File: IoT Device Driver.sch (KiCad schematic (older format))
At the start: 10 parts

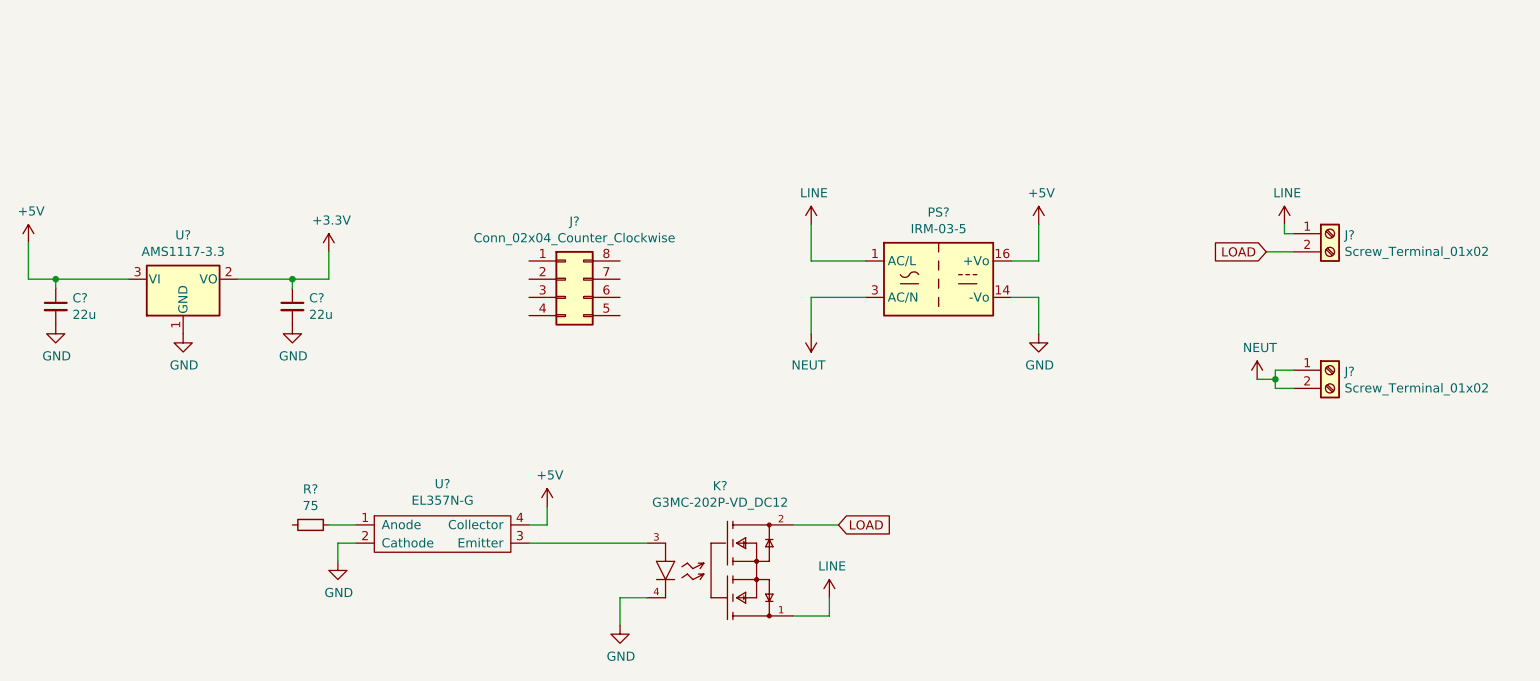
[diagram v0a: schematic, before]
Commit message: assignment of footprint over except optocoupler
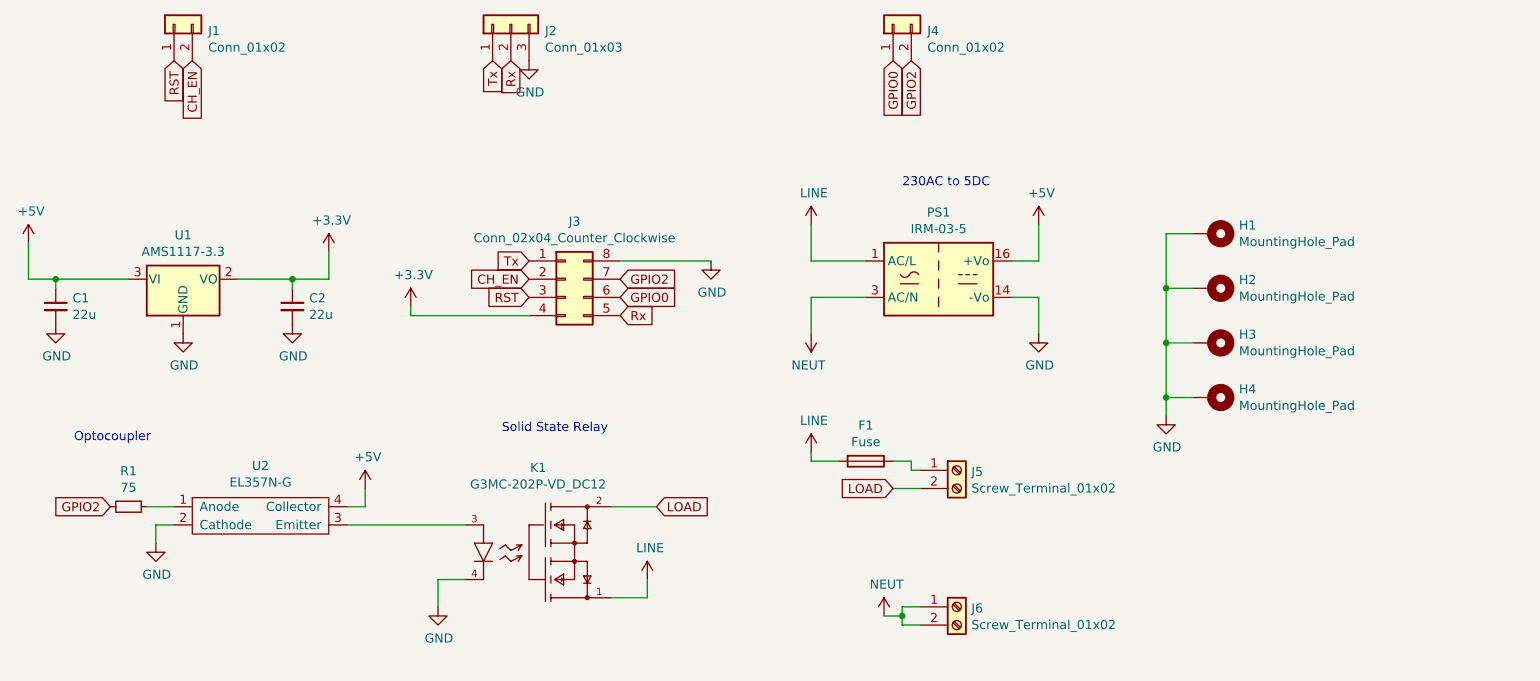
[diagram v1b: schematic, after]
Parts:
- added F1: Fuse, Fuse:Fuseholder_Cylinder-5x20mm_EATON_H15-V-1_Vertical_Closed, symbol Device:Fuse
- added H1, H2, H3, H4: MountingHole_Pad, MountingHole:MountingHole_4.3mm_M4_Pad_Via, symbol Mechanical:MountingHole_Pad
- added J1, J4: Conn_01x02, Connector_PinHeader_2.54mm:PinHeader_1x02_P2.54mm_Vertical, symbol Connector_Generic:Conn_01x02
- added J2: Conn_01x03, Connector_PinHeader_2.54mm:PinHeader_1x03_P2.54mm_Vertical, symbol Connector_Generic:Conn_01x03
- C1, C2: renamed from C?; footprint (none) -> Capacitor_SMD:C_0603_1608Metric
- J3: renamed from J?; footprint (none) -> Connector_PinHeader_2.54mm:PinHeader_2x04_P2.54mm_Vertical
- J5, J6: renamed from J?; footprint (none) -> TerminalBlock_Phoenix:TerminalBlock_Phoenix_PT-1,5-2-5.0-H_1x02_P5.00mm_Horizontal
- R1: renamed from R?; footprint (none) -> Resistor_SMD:R_1206_3216Metric
- gave numbers to parts that had none: 4
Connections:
- net +3V3: now also J3.4 (Pin_4)
- net GND: now also J3.8 (Pin_8), H1.1, H2.1, H3.1, H4.1, J2.3 (Pin_3)
- net LINE: now also F1.2; no longer J5.1 (Pin_1)
- net Tx: now reaches J3.1 (Pin_1)
- net Tx: now also J2.1 (Pin_1)
- net CH_EN: now reaches J3.2 (Pin_2)
- net CH_EN: now also J1.2 (Pin_2)
- net RST: now reaches J3.3 (Pin_3)
- net RST: now also J1.1 (Pin_1)
- net Rx: now reaches J3.5 (Pin_5)
- net Rx: now also J2.2 (Pin_2)
- net GPIO0: now reaches J3.6 (Pin_6)
- net GPIO0: now also J4.1 (Pin_1)
- net GPIO2: now reaches J3.7 (Pin_7)
- net GPIO2: now also R1.2, J4.2 (Pin_2)
- new net: F1.1, J5.1 (Pin_1)
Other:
- note added: "230AC to 5DC"
- note added: "Optocoupler"
- note added: "Solid State Relay"
- moved on the sheet: J5, J6, K1, R1, U2

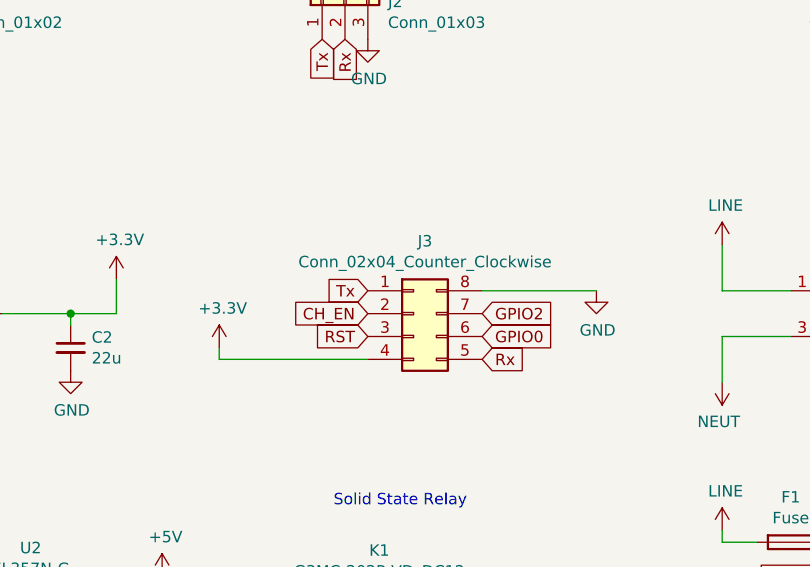
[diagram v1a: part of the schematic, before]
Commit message: Components alignment in PCB
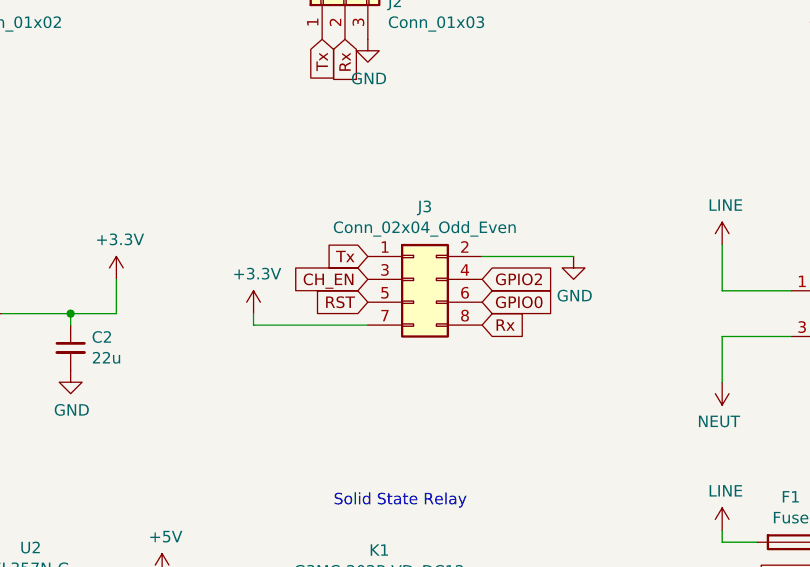
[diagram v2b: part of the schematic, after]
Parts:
- removed J3: Conn_02x04_Counter_Clockwise, Connector_PinHeader_2.54mm:PinHeader_2x04_P2.54mm_Vertical, symbol Connector_Generic:Conn_02x04_Counter_Clockwise
- added J3: Conn_02x04_Odd_Even, Connector_PinHeader_2.54mm:PinHeader_2x04_P2.54mm_Vertical, symbol Connector_Generic:Conn_02x04_Odd_Even
- F1: footprint Fuse:Fuseholder_Cylinder-5x20mm_EATON_H15-V-1_Vertical_Closed -> Fuse:Fuseholder_Cylinder-5x20mm_Schurter_0031_8201_Horizontal_Open
- K1: footprint Omron-G3MC-202P-VD_DC12-* -> eec:Omron-G3MC-202P-VD_DC12-MFG
- U2: footprint (none) -> saranyan:EL357N_G-2.54SOP4P
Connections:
- net +3V3: now also J3.7 (Pin_7)
- net CH_EN: now also J3.3 (Pin_3)
- net GND: now also J3.2 (Pin_2)
- net GPIO0: now also J3.6 (Pin_6)
- net GPIO2: now also J3.4 (Pin_4)
- net RST: now also J3.5 (Pin_5)
- net Rx: now also J3.8 (Pin_8)
- net Tx: now also J3.1 (Pin_1)
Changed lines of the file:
@@
 $EndDescr
-$Comp
-L Connector_Generic:Conn_02x04_Counter_Clockwise J3
-U 1 1 6144891D
-P 5100 3200
-F 0 "J3" H 5150 3517 50  0000 C CNN
-F 1 "Conn_02x04_Counter_Clockwise" H 5150 3426 50  0000 C CNN
-F 2 "Connector_PinHeader_2.54mm:PinHeader_2x04_P2.54mm_Vertical" H 5100 3200 50  0001 C CNN
-F 3 "~" H 5100 3200 50  0001 C CNN
-	1    5100 3200
-	1    0    0    -1
-$EndComp
 $Comp
 L Regulator_Linear:AMS1117-3.3 U1
@@
 F 0 "K1" H 4950 4864 50  0000 C CNN
 F 1 "G3MC-202P-VD_DC12" H 4950 4773 50  0000 C CNN
-F 2 "Omron-G3MC-202P-VD_DC12-*" H 4450 5050 50  0001 L CNN
+F 2 "eec:Omron-G3MC-202P-VD_DC12-MFG" H 4450 5050 50  0001 L CNN
 F 3 "https://omronfs.omron.com/en_US/ecb/products/pdf/en-g3mc.pdf" H 4450 5150 50  0001 L CNN
 F 4 "+80°C" H 4450 5250 50  0001 L CNN "ambient temperature range high"
@@
 F 0 "U2" H 3425 4775 50  0000 C CNN
 F 1 "EL357N-G" H 3425 4684 50  0000 C CNN
-F 2 "" H 3400 4500 50  0001 C CNN
+F 2 "saranyan:EL357N_G-2.54SOP4P" H 3400 4500 50  0001 C CNN
 F 3 "" H 3400 4500 50  0001 C CNN
 	1    3400 4500
@@
 Wire Wire Line
 	6900 4350 7050 4350
-$Comp
-L power:+3.3V #PWR08
-U 1 1 6148FED5
-P 4250 3350
-F 0 "#PWR08" H 4250 3200 50  0001 C CNN
-F 1 "+3.3V" H 4265 3523 50  0000 C CNN
-F 2 "" H 4250 3350 50  0001 C CNN
-F 3 "" H 4250 3350 50  0001 C CNN
-	1    4250 3350
-	1    0    0    -1
-$EndComp
-Wire Wire Line
-	4250 3350 4250 3400
-Wire Wire Line
-	4250 3400 4900 3400
 Text GLabel 4700 2000 3    50   Input ~ 0
-Tx
-Text GLabel 4900 3100 0    50   Input ~ 0
 Tx
 Text GLabel 4800 2000 3    50   Input ~ 0
 Rx
-Text GLabel 5400 3400 2    50   Input ~ 0
-Rx
 Text GLabel 6900 2000 3    50   Input ~ 0
-GPIO0
-Text GLabel 5400 3300 2    50   Input ~ 0
 GPIO0
 Text GLabel 7000 2000 3    50   Input ~ 0
 GPIO2
-Text GLabel 5400 3200 2    50   Input ~ 0
-GPIO2
 Text GLabel 2600 4450 0    50   Input ~ 0
 GPIO2
-Text GLabel 4900 3300 0    50   Input ~ 0
-RST
-$Comp
-L power:GND #PWR012
-U 1 1 61495F70
-P 5900 3100
-F 0 "#PWR012" H 5900 2850 50  0001 C CNN
-F 1 "GND" H 5905 2927 50  0000 C CNN
-F 2 "" H 5900 3100 50  0001 C CNN
-F 3 "" H 5900 3100 50  0001 C CNN
-	1    5900 3100
-	1    0    0    -1
-$EndComp
-Wire Wire Line
-	5400 3100 5900 3100
-Text GLabel 4900 3200 0    50   Input ~ 0
-CH_EN
 Text GLabel 2950 2000 3    50   Input ~ 0
 RST
@@
 F 0 "F1" V 6553 4200 50  0000 C CNN
 F 1 "Fuse" V 6644 4200 50  0000 C CNN
-F 2 "Fuse:Fuseholder_Cylinder-5x20mm_EATON_H15-V-1_Vertical_Closed" V 6680 4200 50  0001 C CNN
+F 2 "Fuse:Fuseholder_Cylinder-5x20mm_Schurter_0031_8201_Horizontal_Open" V 6680 4200 50  0001 C CNN
 F 3 "~" H 6750 4200 50  0001 C CNN
 	1    6750 4200
@@
 Wire Wire Line
 	6900 4200 7000 4200
+Text GLabel 4900 3150 0    50   Input ~ 0
+RST
+$Comp
+L Connector_Generic:Conn_02x04_Odd_Even J3
+U 1 1 614E39E6
+P 5100 3050
+F 0 "J3" H 5150 3367 50  0000 C CNN
+F 1 "Conn_02x04_Odd_Even" H 5150 3276 50  0000 C CNN
+F 2 "Connector_PinHeader_2.54mm:PinHeader_2x04_P2.54mm_Vertical" H 5100 3050 50  0001 C CNN
+F 3 "~" H 5100 3050 50  0001 C CNN
+	1    5100 3050
+	1    0    0    -1
+$EndComp
+Text GLabel 4900 2950 0    50   Input ~ 0
+Tx
+Text GLabel 4900 3050 0    50   Input ~ 0
+CH_EN
+$Comp
+L power:+3.3V #PWR08
+U 1 1 614E4A4D
+P 4400 3200
+F 0 "#PWR08" H 4400 3050 50  0001 C CNN
+F 1 "+3.3V" H 4415 3373 50  0000 C CNN
+F 2 "" H 4400 3200 50  0001 C CNN
+F 3 "" H 4400 3200 50  0001 C CNN
+	1    4400 3200
+	1    0    0    -1
+$EndComp
+Text GLabel 5400 3050 2    50   Input ~ 0
+GPIO2
+Text GLabel 5400 3150 2    50   Input ~ 0
+GPIO0
+Text GLabel 5400 3250 2    50   Input ~ 0
+Rx
+$Comp
+L power:GND #PWR012
+U 1 1 614E6EBE
+P 5800 2950
+F 0 "#PWR012" H 5800 2700 50  0001 C CNN
+F 1 "GND" H 5805 2777 50  0000 C CNN
+F 2 "" H 5800 2950 50  0001 C CNN
+F 3 "" H 5800 2950 50  0001 C CNN
+	1    5800 2950
+	1    0    0    -1
+$EndComp
+Wire Wire Line
+	5400 2950 5800 2950
+Wire Wire Line
+	4400 3200 4400 3250
+Wire Wire Line
+	4400 3250 4900 3250
 $EndSCHEMATC

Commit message: Routing
Routing for low power components over. Things to do: 1)Edit copper fill area, 2(Calculate track width for 3A, 3)Lay track for high power components on bottom layer only
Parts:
- PS1: footprint Converter_ACDC:Converter_ACDC_MeanWell_IRM-03-xx_THT -> Converter_ACDC:Converter_ACDC_MeanWell_IRM-03-xx_SMD
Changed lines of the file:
@@
 F 0 "PS1" H 7150 3567 50  0000 C CNN
 F 1 "IRM-03-5" H 7150 3476 50  0000 C CNN
-F 2 "Converter_ACDC:Converter_ACDC_MeanWell_IRM-03-xx_THT" H 7150 2850 50  0001 C CNN
+F 2 "Converter_ACDC:Converter_ACDC_MeanWell_IRM-03-xx_SMD" H 7150 2850 50  0001 C CNN
 F 3 "https://www.meanwell.com/Upload/PDF/IRM-03/IRM-03-SPEC.PDF" H 7150 2800 50  0001 C CNN
 	1    7150 3200

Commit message: PCB Version 1.0 over
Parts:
- added J7: Conn_01x06, Connector_PinSocket_2.54mm:PinSocket_1x06_P2.54mm_Vertical, symbol Connector_Generic:Conn_01x06
- J1, J4: footprint Connector_PinHeader_2.54mm:PinHeader_1x02_P2.54mm_Vertical -> Connector_PinSocket_2.54mm:PinSocket_1x02_P2.54mm_Vertical
- J2: footprint Connector_PinHeader_2.54mm:PinHeader_1x03_P2.54mm_Vertical -> Connector_PinSocket_2.54mm:PinSocket_1x03_P2.54mm_Vertical
- K1: value G3MC-202P-VD_DC12 -> G3MC-202P-VD_DC5
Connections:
- net +3V3: now also J7.3 (Pin_3), J7.4 (Pin_4)
- net +5V: now also J7.1 (Pin_1), J7.2 (Pin_2)
- net GND: now also J7.5 (Pin_5), J7.6 (Pin_6)
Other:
- moved on the sheet: J1, J2, J4
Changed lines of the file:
@@
 P 4450 4550
 F 0 "K1" H 4950 4864 50  0000 C CNN
-F 1 "G3MC-202P-VD_DC12" H 4950 4773 50  0000 C CNN
+F 1 "G3MC-202P-VD_DC5" H 4950 4773 50  0000 C CNN
 F 2 "eec:Omron-G3MC-202P-VD_DC12-MFG" H 4450 5050 50  0001 L CNN
 F 3 "https://omronfs.omron.com/en_US/ecb/products/pdf/en-g3mc.pdf" H 4450 5150 50  0001 L CNN
@@
 Wire Wire Line
 	6900 4350 7050 4350
-Text GLabel 4700 2000 3    50   Input ~ 0
+Text GLabel 3900 2000 3    50   Input ~ 0
 Tx
-Text GLabel 4800 2000 3    50   Input ~ 0
+Text GLabel 4000 2000 3    50   Input ~ 0
 Rx
-Text GLabel 6900 2000 3    50   Input ~ 0
+Text GLabel 5200 2000 3    50   Input ~ 0
 GPIO0
-Text GLabel 7000 2000 3    50   Input ~ 0
+Text GLabel 5300 2000 3    50   Input ~ 0
 GPIO2
 Text GLabel 2600 4450 0    50   Input ~ 0
 GPIO2
-Text GLabel 2950 2000 3    50   Input ~ 0
+Text GLabel 2500 2000 3    50   Input ~ 0
 RST
-Text GLabel 3050 2000 3    50   Input ~ 0
+Text GLabel 2600 2000 3    50   Input ~ 0
 CH_EN
 $Comp
 L power:GND #PWR010
 U 1 1 614974B0
-P 4900 2000
-F 0 "#PWR010" H 4900 1750 50  0001 C CNN
-F 1 "GND" H 4905 1827 50  0000 C CNN
-F 2 "" H 4900 2000 50  0001 C CNN
-F 3 "" H 4900 2000 50  0001 C CNN
-	1    4900 2000
+P 4100 2000
+F 0 "#PWR010" H 4100 1750 50  0001 C CNN
+F 1 "GND" H 4105 1827 50  0000 C CNN
+F 2 "" H 4100 2000 50  0001 C CNN
+F 3 "" H 4100 2000 50  0001 C CNN
+	1    4100 2000
 	1    0    0    -1
 $EndComp
@@
 L Connector_Generic:Conn_01x02 J1
 U 1 1 614A936D
-P 2950 1800
-F 0 "J1" V 2914 1612 50  0000 R CNN
-F 1 "Conn_01x02" V 2823 1612 50  0000 R CNN
-F 2 "Connector_PinHeader_2.54mm:PinHeader_1x02_P2.54mm_Vertical" H 2950 1800 50  0001 C CNN
-F 3 "~" H 2950 1800 50  0001 C CNN
-	1    2950 1800
+P 2500 1800
+F 0 "J1" V 2464 1612 50  0000 R CNN
+F 1 "Conn_01x02" V 2373 1612 50  0000 R CNN
+F 2 "Connector_PinSocket_2.54mm:PinSocket_1x02_P2.54mm_Vertical" H 2500 1800 50  0001 C CNN
+F 3 "~" H 2500 1800 50  0001 C CNN
+	1    2500 1800
 	0    -1   -1   0
 $EndComp
@@
 L Connector_Generic:Conn_01x02 J4
 U 1 1 614A9BB4
-P 6900 1800
-F 0 "J4" V 6864 1612 50  0000 R CNN
-F 1 "Conn_01x02" V 6773 1612 50  0000 R CNN
-F 2 "Connector_PinHeader_2.54mm:PinHeader_1x02_P2.54mm_Vertical" H 6900 1800 50  0001 C CNN
-F 3 "~" H 6900 1800 50  0001 C CNN
-	1    6900 1800
+P 5200 1800
+F 0 "J4" V 5164 1612 50  0000 R CNN
+F 1 "Conn_01x02" V 5073 1612 50  0000 R CNN
+F 2 "Connector_PinSocket_2.54mm:PinSocket_1x02_P2.54mm_Vertical" H 5200 1800 50  0001 C CNN
+F 3 "~" H 5200 1800 50  0001 C CNN
+	1    5200 1800
 	0    -1   -1   0
 $EndComp
@@
 L Connector_Generic:Conn_01x03 J2
 U 1 1 614AA5E9
-P 4800 1800
-F 0 "J2" V 4764 1612 50  0000 R CNN
-F 1 "Conn_01x03" V 4673 1612 50  0000 R CNN
-F 2 "Connector_PinHeader_2.54mm:PinHeader_1x03_P2.54mm_Vertical" H 4800 1800 50  0001 C CNN
-F 3 "~" H 4800 1800 50  0001 C CNN
-	1    4800 1800
+P 4000 1800
+F 0 "J2" V 3964 1612 50  0000 R CNN
+F 1 "Conn_01x03" V 3873 1612 50  0000 R CNN
+F 2 "Connector_PinSocket_2.54mm:PinSocket_1x03_P2.54mm_Vertical" H 4000 1800 50  0001 C CNN
+F 3 "~" H 4000 1800 50  0001 C CNN
+	1    4000 1800
 	0    -1   -1   0
 $EndComp
@@
 Wire Wire Line
 	4400 3250 4900 3250
+$Comp
+L Connector_Generic:Conn_01x06 J7
+U 1 1 6151AA3C
+P 6700 1800
+F 0 "J7" V 6664 1412 50  0000 R CNN
+F 1 "Conn_01x06" V 6573 1412 50  0000 R CNN
+F 2 "Connector_PinSocket_2.54mm:PinSocket_1x06_P2.54mm_Vertical" H 6700 1800 50  0001 C CNN
+F 3 "~" H 6700 1800 50  0001 C CNN
+	1    6700 1800
+	0    -1   -1   0
+$EndComp
+$Comp
+L power:+3.3V #PWR022
+U 1 1 6151C48B
+P 6700 2100
+F 0 "#PWR022" H 6700 1950 50  0001 C CNN
+F 1 "+3.3V" V 6700 2350 50  0000 C CNN
+F 2 "" H 6700 2100 50  0001 C CNN
+F 3 "" H 6700 2100 50  0001 C CNN
+	1    6700 2100
+	-1   0    0    1
+$EndComp
+$Comp
+L power:+3.3V #PWR023
+U 1 1 6151F1E6
+P 6800 2100
+F 0 "#PWR023" H 6800 1950 50  0001 C CNN
+F 1 "+3.3V" V 6800 2350 50  0000 C CNN
+F 2 "" H 6800 2100 50  0001 C CNN
+F 3 "" H 6800 2100 50  0001 C CNN
+	1    6800 2100
+	-1   0    0    1
+$EndComp
+$Comp
+L power:+5V #PWR021
+U 1 1 6151F7D4
+P 6600 2100
+F 0 "#PWR021" H 6600 1950 50  0001 C CNN
+F 1 "+5V" V 6600 2300 50  0000 C CNN
+F 2 "" H 6600 2100 50  0001 C CNN
+F 3 "" H 6600 2100 50  0001 C CNN
+	1    6600 2100
+	-1   0    0    1
+$EndComp
+$Comp
+L power:+5V #PWR020
+U 1 1 61520689
+P 6500 2100
+F 0 "#PWR020" H 6500 1950 50  0001 C CNN
+F 1 "+5V" V 6500 2300 50  0000 C CNN
+F 2 "" H 6500 2100 50  0001 C CNN
+F 3 "" H 6500 2100 50  0001 C CNN
+	1    6500 2100
+	-1   0    0    1
+$EndComp
+$Comp
+L power:GND #PWR024
+U 1 1 6152252F
+P 6900 2100
+F 0 "#PWR024" H 6900 1850 50  0001 C CNN
+F 1 "GND" V 6900 1900 50  0000 C CNN
+F 2 "" H 6900 2100 50  0001 C CNN
+F 3 "" H 6900 2100 50  0001 C CNN
+	1    6900 2100
+	1    0    0    -1
+$EndComp
+$Comp
+L power:GND #PWR025
+U 1 1 61522993
+P 7000 2100
+F 0 "#PWR025" H 7000 1850 50  0001 C CNN
+F 1 "GND" V 7000 1900 50  0000 C CNN
+F 2 "" H 7000 2100 50  0001 C CNN
+F 3 "" H 7000 2100 50  0001 C CNN
+	1    7000 2100
+	1    0    0    -1
+$EndComp
+Wire Wire Line
+	6500 2000 6500 2100
+Wire Wire Line
+	6600 2000 6600 2100
+Wire Wire Line
+	6700 2000 6700 2100
+Wire Wire Line
+	6800 2000 6800 2100
+Wire Wire Line
+	6900 2000 6900 2100
+Wire Wire Line
+	7000 2000 7000 2100
 $EndSCHEMATC
